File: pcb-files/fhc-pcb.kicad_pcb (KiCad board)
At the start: 2 copper layers, 133.3 x 63.5 mm, 23 parts, among them J1 Screw_Terminal_01x02, SW1 SW_Push_Dual, SW2 SW_Push_Dual, SW3 SW_Push_Dual, SW4 SW_Push_Dual, SW5 SW_Push_Dual, SW7 SW_Push, U1 WeMos_D1_mini, U2 AMS1117_Shield_AZDelivery

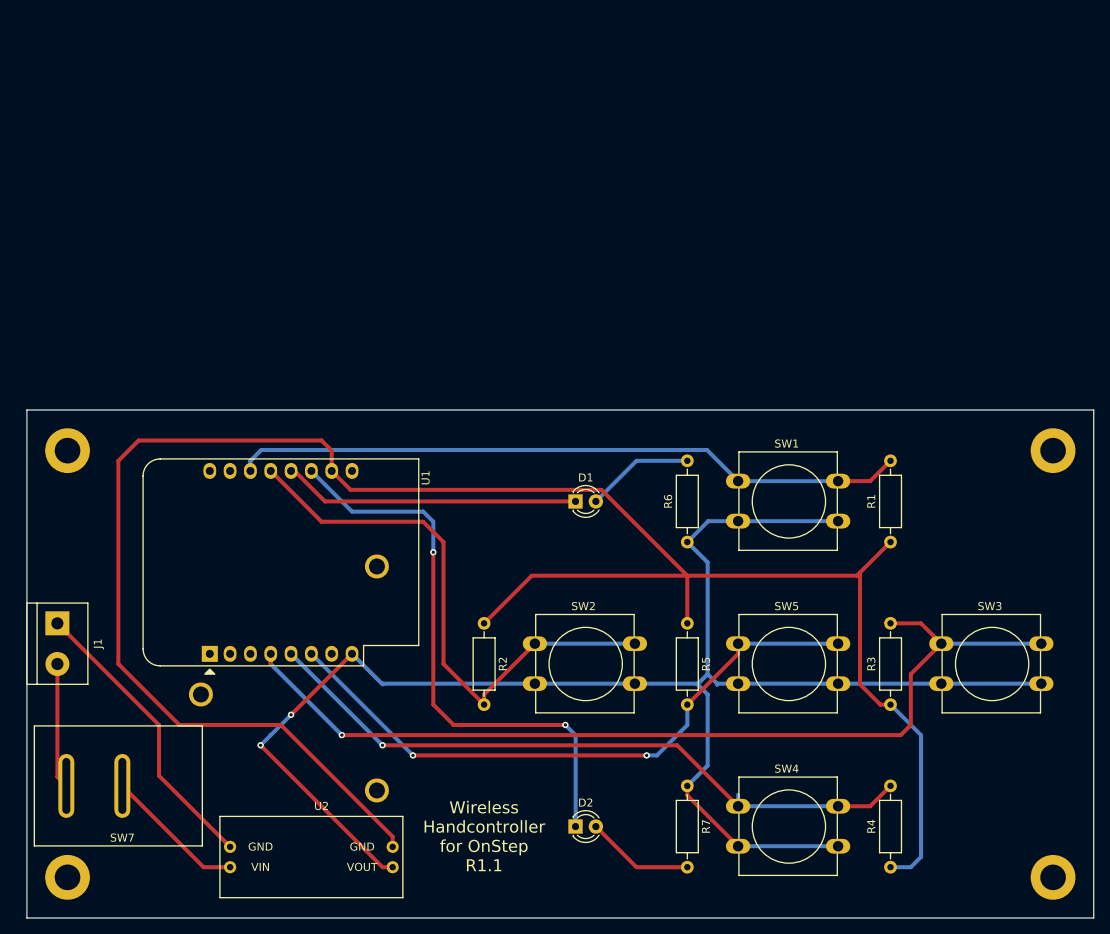
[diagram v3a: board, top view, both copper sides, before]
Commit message: Pinmap and PCB Update
Added PINMAP for R1 PCB
Added OLED display to PCB for R2
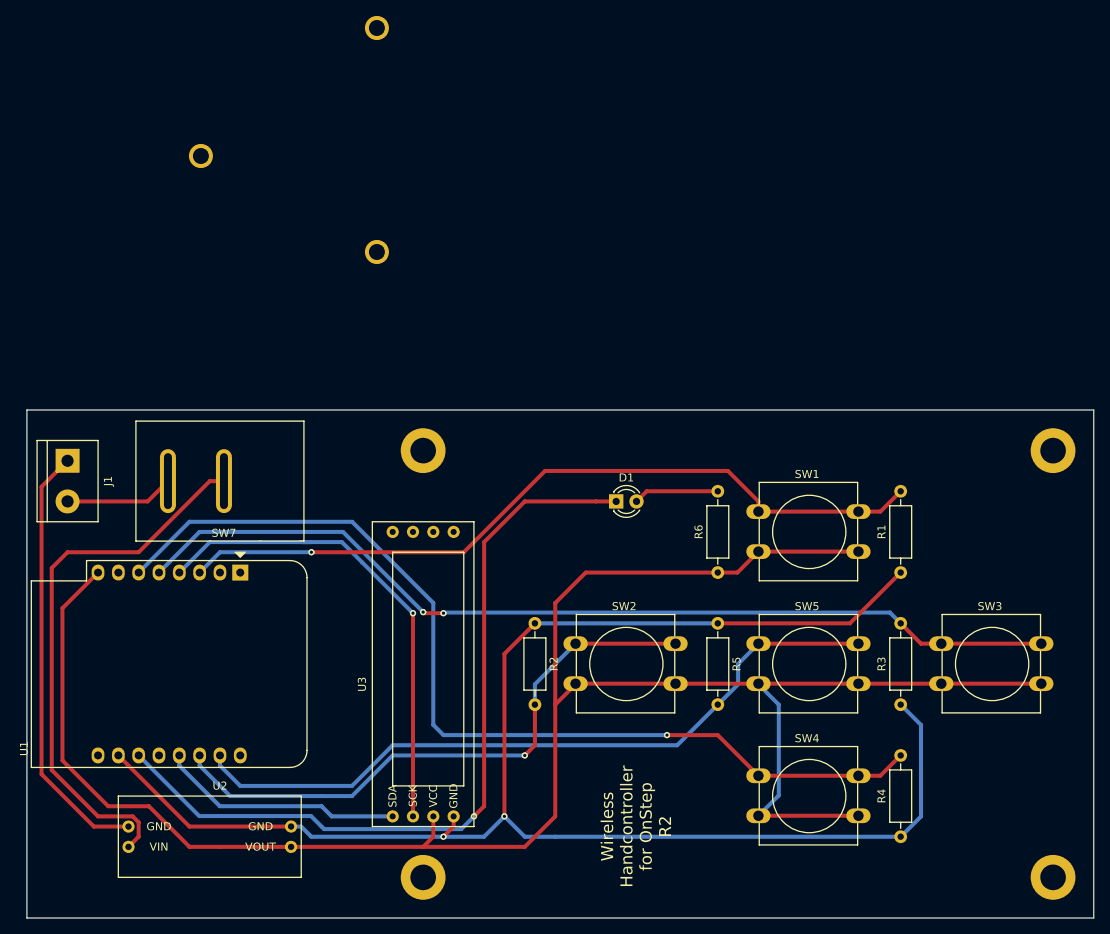
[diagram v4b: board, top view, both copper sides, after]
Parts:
- removed D2: LED, LED_THT:LED_D3.0mm
- removed R7: R, Resistor_THT:R_Axial_DIN0207_L6.3mm_D2.5mm_P10.16mm_Horizontal
- removed the REF** at (100.3, 68.6)
- removed the REF** at (100.3, 121.9)
- added REF**: MountingHole_3.2mm_M3_DIN965_Pad, MountingHole:MountingHole_3.2mm_M3_DIN965_Pad, F.Cu at (144.8, 121.9)
- added REF**: MountingHole_3.2mm_M3_DIN965_Pad, MountingHole:MountingHole_3.2mm_M3_DIN965_Pad, F.Cu at (144.8, 68.6)
- added U3: OLED_0.91_AZDelivery, Personal Library:OLED_0.91_AZDelivery, F.Cu at (144.8, 97.8)
- R6: value R -> 150
- moved REF** 67.3 mm to (127.0, 31.8)
- moved SW7 40.2 mm to (119.4, 72.4)
- moved J1 20.4 mm to (100.3, 69.8)
- moved U2 13.0 mm to (119.4, 116.8)
- moved U1 10.9 mm to (121.9, 83.8), turned to 270 degrees
- moved R2 6.35 mm to (158.8, 90.2)
- moved R6 5.39 mm to (181.6, 83.8)
- moved SW2 5.08 mm to (163.8, 92.7)
- moved D1 5.08 mm to (168.9, 74.9)
- moved SW1 4.58 mm to (186.7, 76.2)
- moved SW4 4.58 mm to (186.7, 109.2)
- moved R4 4.02 mm to (204.5, 116.8)
- moved R1 4.02 mm to (204.5, 83.8)
- moved R5 3.81 mm to (181.6, 90.2)
- moved SW5 2.54 mm to (186.7, 92.7)
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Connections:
- U1 pad 11: Net-(D2-Pad1) -> Net-(D1-Pad1)
- U1 pad 12: Net-(D1-Pad1) -> Net-(U1-Pad12)
- U1 pad 13: Net-(R2-Pad2) -> Net-(U1-Pad13)
- U1 pad 14: Net-(R1-Pad2) -> Net-(R2-Pad2)
- U1 pad 15: Net-(U1-Pad15) -> Net-(R5-Pad2)
- U1 pad 3: Net-(U1-Pad3) -> Net-(R1-Pad2)
- U1 pad 4: Net-(R3-Pad2) -> Net-(U1-Pad4)
- U1 pad 5: Net-(R4-Pad2) -> Net-(R3-Pad2)
- U1 pad 6: Net-(R5-Pad2) -> Net-(R4-Pad2)
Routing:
- net Net-(D2-Pad1): track 71.5 -> 0.00 mm, vias 2 -> 0
- net Net-(D1-Pad1): track 37.1 -> 99.8 mm, vias 0 -> 1
- net Net-(U1-Pad4): track 0.00 -> 61.1 mm, vias 0 -> 1
- net +9V: track 255.3 -> 199.8 mm, vias 0 -> 2
- net Net-(R6-Pad1): track 202.5 -> 257.6 mm, vias 2 -> 0
- net Net-(SW7-Pad2): track 17.7 -> 68.9 mm
- net Net-(R4-Pad2): track 85.7 -> 121.0 mm
- net Net-(U1-Pad13): track 0.00 -> 30.6 mm
- net Net-(J1-Pad1): track 36.9 -> 54.1 mm
- net Net-(D2-Pad2): track 13.5 -> 0.00 mm
- net Net-(R1-Pad2): track 84.5 -> 96.8 mm, vias 0 -> 1
- net Net-(R5-Pad2): track 79.1 -> 91.0 mm, vias 2 -> 0
- net Net-(R2-Pad2): track 70.4 -> 74.7 mm, vias 0 -> 1
- net Net-(D1-Pad2): track 13.5 -> 10.7 mm
- net Net-(J1-Pad2): track 15.7 -> 13.6 mm
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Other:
- board text added: "Wireless Handcontroller for OnStep R2"
- board text removed: "Wireless Handcontroller for OnStep R1.1"

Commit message: PCB Updates
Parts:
- SW7: footprint Personal Library:Wippschalter -> Connector_Molex:Molex_KK-254_AE-6410-02A_1x02_P2.54mm_Vertical
- U1: footprint Module:WEMOS_D1_mini_light -> Personal Library:WEMOS_D1_Mini
- moved SW7 2.84 mm to (120.7, 69.8), turned to 270 degrees
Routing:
- net Net-(J1-Pad2): track 13.6 -> 22.4 mm

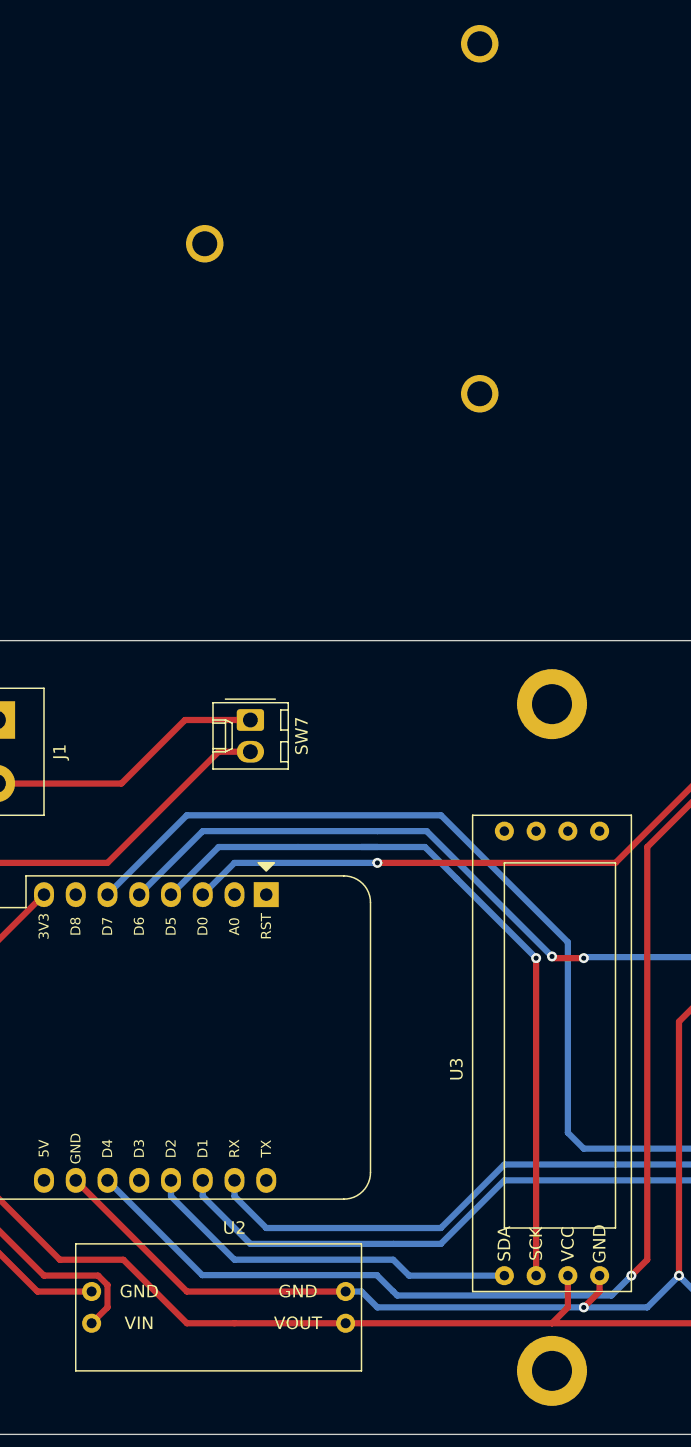
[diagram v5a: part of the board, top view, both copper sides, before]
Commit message: Cleaned up PCB structure
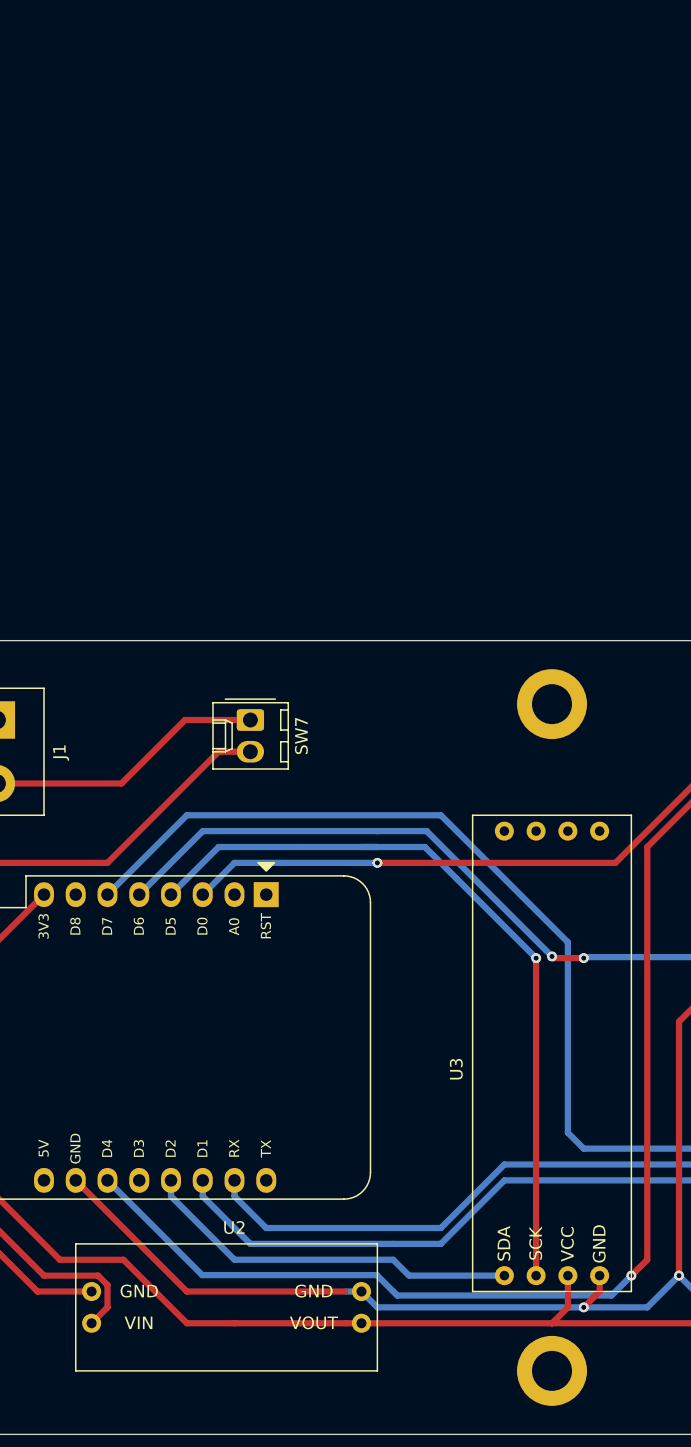
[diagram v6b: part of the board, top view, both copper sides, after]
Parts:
- removed the REF** at (127.0, 31.8)
- U1: footprint Personal Library:WEMOS_D1_Mini -> whc_pcb-files:WEMOS_D1_Mini
- U2: footprint Personal Library:AMS1117_Shield_AZDelivery -> whc_pcb-files:AMS1117_Shield_AZDelivery
- U3: footprint Personal Library:OLED_0.91_AZDelivery -> whc_pcb-files:OLED_0.91_AZDelivery

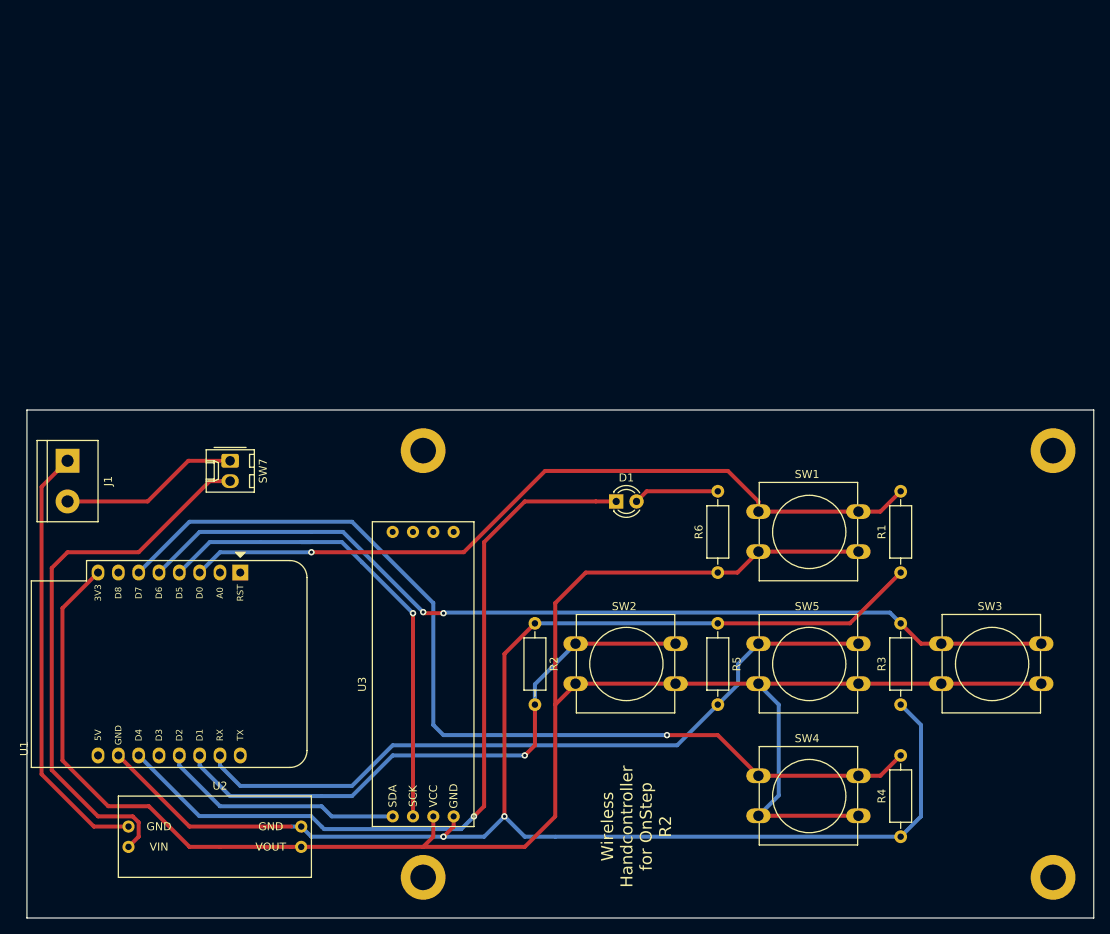
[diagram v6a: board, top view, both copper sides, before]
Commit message: Added GND plane to PCB
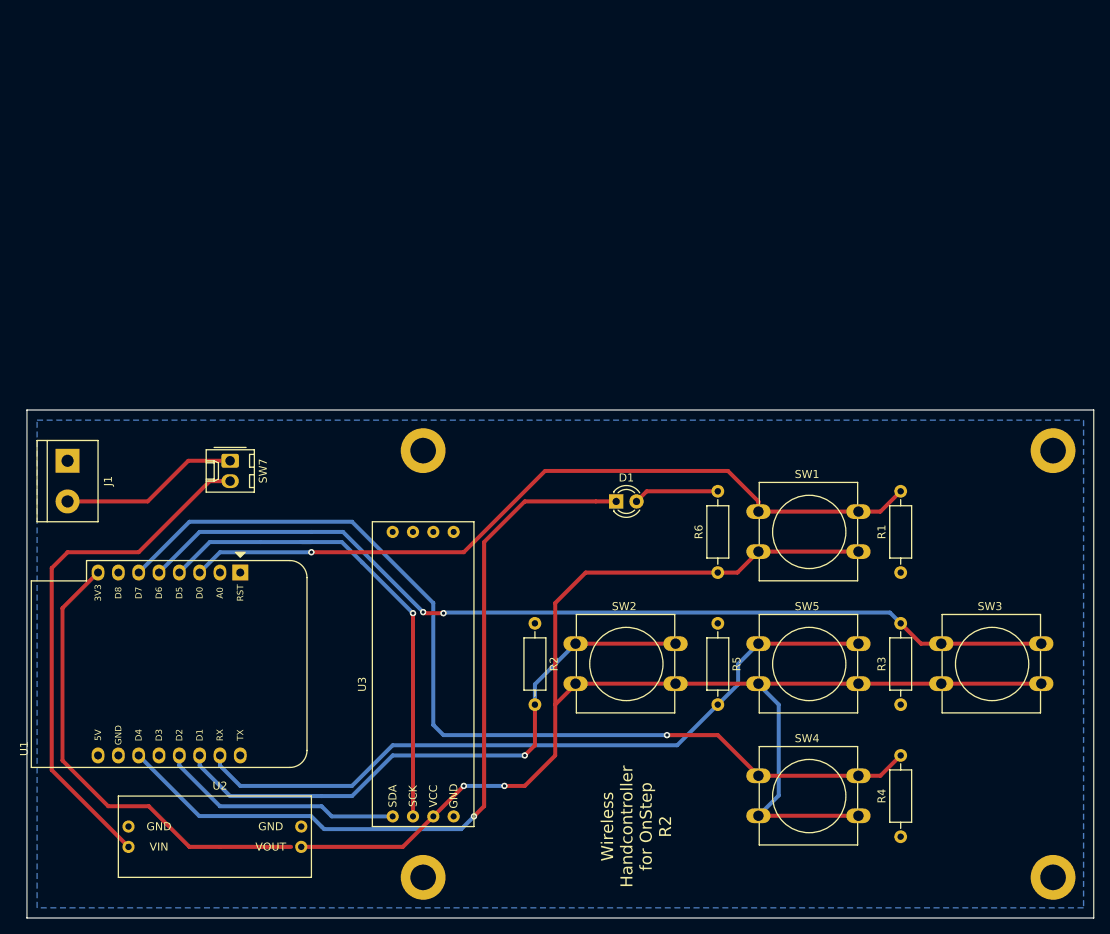
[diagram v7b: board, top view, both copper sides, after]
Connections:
- net Net-(R6-Pad1) renamed +3V3
- J1 pad 1: Net-(J1-Pad1) -> GND
- R1 pad 1: +9V -> GND
- R2 pad 1: +9V -> GND
- R3 pad 1: +9V -> GND
- R4 pad 1: +9V -> GND
- R5 pad 1: +9V -> GND
- SW7 pad 2: Net-(SW7-Pad2) -> +9V
- U1 pad 10: +9V -> GND
- U2 pad 1: Net-(SW7-Pad2) -> +9V
- U2 pad 2: Net-(J1-Pad1) -> GND
- U2 pad 3: +9V -> GND
- U3 pad 1: +9V -> GND
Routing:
- net +9V: track 199.8 -> 65.6 mm, vias 2 -> 0
- net Net-(SW7-Pad2): track 69.2 -> 0.00 mm
- net Net-(J1-Pad1): track 54.1 -> 0.00 mm
- net +3V3: track 257.6 -> 247.6 mm, vias 0 -> 2
- added copper zone on B.Cu, net GND

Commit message: PCB R2 incl. gerbers
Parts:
- removed the REF** at (144.8, 121.9)
- removed U2: AMS1117_Shield_AZDelivery, whc_pcb-files:AMS1117_Shield_AZDelivery
- added REF**: MountingHole_3.2mm_M3_DIN965_Pad, MountingHole:MountingHole_3.2mm_M3_DIN965_Pad, F.Cu at (176.5, 73.7)
- added REF**: MountingHole_3.2mm_M3_DIN965_Pad, MountingHole:MountingHole_3.2mm_M3_DIN965_Pad, F.Cu at (176.5, 117.2)
- added REF**: MountingHole_3.2mm_M3_DIN965_Pad, MountingHole:MountingHole_3.2mm_M3_DIN965_Pad, F.Cu at (114.3, 121.9)
- moved SW7 53.8 mm to (102.9, 120.7), turned to 90 degrees
- moved REF** 30.5 mm to (114.3, 68.6)
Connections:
- net +3V3 renamed Net-(R6-Pad1)
- SW7 pad 2: +9V -> +5V
- U1 pad 9: Net-(U1-Pad9) -> +5V
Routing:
- net +9V: track 65.6 -> 0.00 mm
- net Net-(J1-Pad2): track 22.4 -> 48.9 mm
- net +5V: track 0.00 -> 12.0 mm
- net Net-(R1-Pad2): track 96.8 -> 102.6 mm
- net Net-(D1-Pad2): track 10.7 -> 14.6 mm
- net Net-(R6-Pad1): track 247.6 -> 250.1 mm
